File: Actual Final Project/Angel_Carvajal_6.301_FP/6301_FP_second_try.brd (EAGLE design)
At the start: 101.6 x 50.8 mm, 16 parts, among them IC1 MPQ3904, IC2 MPQ3906, IC3 TL072P, IC4 CD4066BE, IC5 LM311N

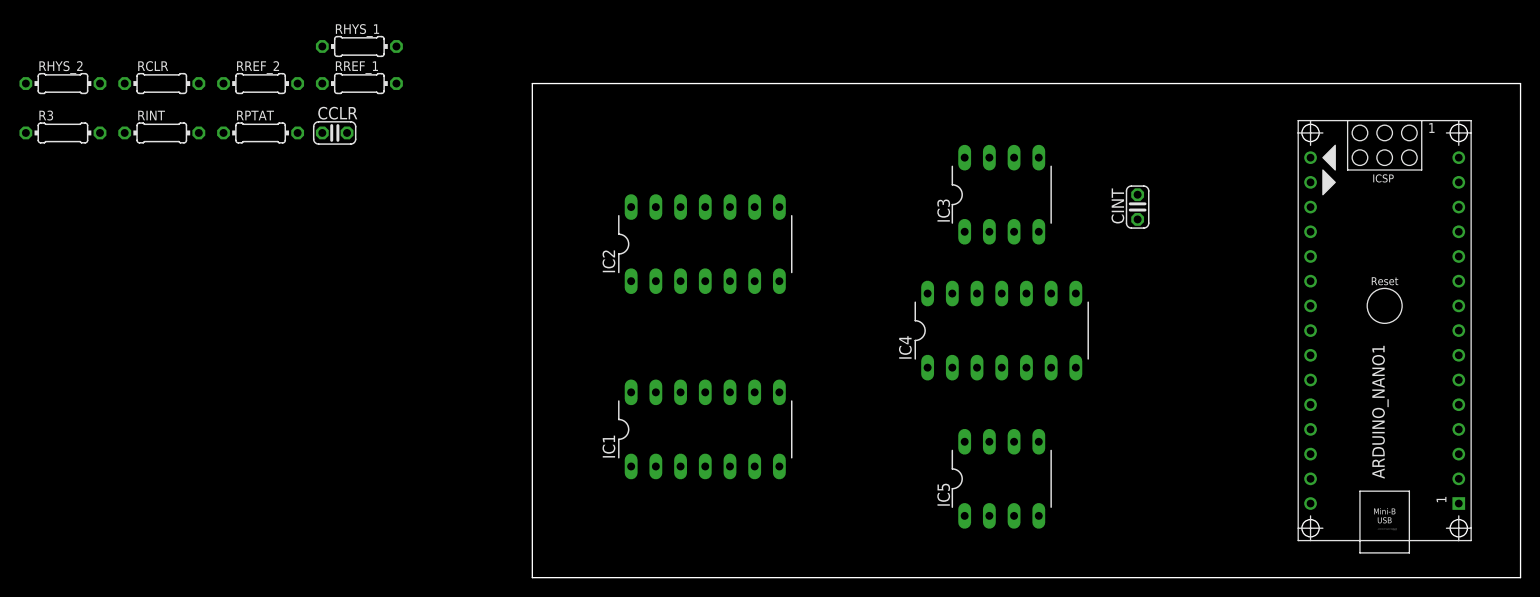
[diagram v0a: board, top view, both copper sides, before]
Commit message: PCB2 Done
-errors on DRC (vias, and something with micro-controller)
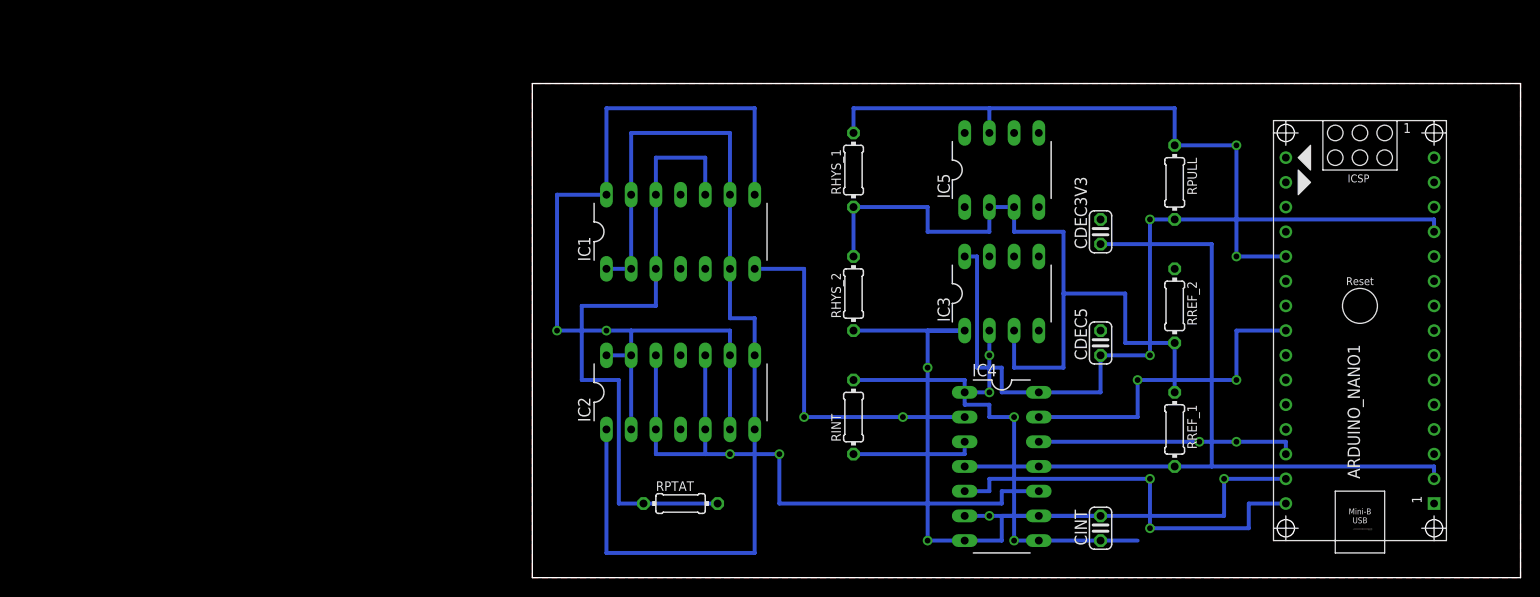
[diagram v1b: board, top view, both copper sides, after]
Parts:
- removed CCLR: (no value), rcl:C025-024X044
- removed R3, RCLR: (no value), rcl:0204/7
- added CDEC3V3, CDEC5: (no value), rcl:C025-024X044
- added RPULL: (no value), rcl:0204/7
- moved RREF_2 96.7 mm to (66.0, 27.9), turned to 270 degrees
- moved RREF_1 91.1 mm to (66.0, 15.2), turned to 270 degrees
- moved RHYS_2 84.1 mm to (33.0, 29.2), turned to 90 degrees
- moved RINT 76.9 mm to (33.0, 16.5), turned to 90 degrees
- moved RPTAT 57.6 mm to (15.2, 7.62)
- moved RHYS_1 52.4 mm to (33.0, 41.9), turned to 90 degrees
- moved CINT 33.2 mm to (58.4, 5.08)
- moved IC5 31.7 mm to (48.3, 41.9)
- moved IC1 20.5 mm to (15.2, 35.6)
- moved IC2 15.5 mm to (15.2, 19.1)
- moved IC4 14.0 mm to (48.3, 11.4), turned to 270 degrees
- moved IC3 10.2 mm to (48.3, 29.2)
- moved ARDUINO_NANO1 2.54 mm to (85.1, 27.9)
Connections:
- removed net CLR: ARDUINO_NANO1.20, ARDUINO_NANO1.25, CCLR.2, IC4.11, IC5.7, R3.1, RCLR.2, RHYS_1.2
- removed net V+: IC3.8
- removed net V-: IC3.4
- new net N$4: ARDUINO_NANO1.20, IC5.7, RHYS_1.2, RPULL.1
- new net START: IC2.10, IC2.12, IC2.3, IC2.5, IC4.10
- new net SW_D: ARDUINO_NANO1.28, IC4.12
- net 3V3: now also CDEC3V3.1, IC4.11; no longer IC2.10, IC2.12, IC2.3, IC2.5
- net 5V: now also CDEC5.1, IC3.8, RPULL.2; no longer R3.2
- net GND: now also CDEC3V3.2, CDEC5.2, IC3.4; no longer CCLR.1, IC4.10, RHYS_2.1
- net N$3: now also IC1.8
- net N$5: now also IC2.7
- net N$6: now also RHYS_2.1; no longer IC5.3
- net SW_A: no longer RCLR.1
- net SW_B: no longer IC4.12
- net SW_C: now also ARDUINO_NANO1.29; no longer ARDUINO_NANO1.28
- net VREF: now also IC5.3
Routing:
- net N$5: track 0.00 -> 100.3 mm
- net N$3: track 0.00 -> 92.7 mm, vias 0 -> 2
- net 3V3: track 0.00 -> 83.8 mm
- net 5V: track 0.00 -> 81.3 mm, vias 0 -> 2
- net VREF: track 0.00 -> 78.7 mm
- net N$2: track 0.00 -> 66.0 mm
- net START: track 0.00 -> 66.0 mm, vias 0 -> 2
- net N$4: track 0.00 -> 64.8 mm, vias 0 -> 2
- net N$6: track 0.00 -> 57.1 mm, vias 0 -> 2
- net N$10: track 0.00 -> 54.6 mm, vias 0 -> 4
- net SW_B: track 0.00 -> 41.9 mm, vias 0 -> 2
- net SW_C: track 0.00 -> 36.8 mm, vias 0 -> 2
- net N$9: track 0.00 -> 36.8 mm, vias 0 -> 2
- net SW_A: track 0.00 -> 34.3 mm, vias 0 -> 2
- net SW_D: track 0.00 -> 26.7 mm, vias 0 -> 2
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- added copper zone on layer 1, net GND
